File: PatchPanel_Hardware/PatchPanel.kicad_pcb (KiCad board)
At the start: 2 copper layers, 172.1 x 75.6 mm, 89 parts, among them Q1 Q_PMOS_DGS, Q10 Q_NMOS_DGS, Q11 Q_NMOS_DGS, Q12 Q_NMOS_DGS, Q13 Q_NMOS_DGS, Q14 Q_NMOS_DGS, Q15 Q_NMOS_DGS, Q16 Q_NMOS_DGS, Q17 Q_PMOS_DGS, Q18 Q_PMOS_DGS, Q19 Q_PMOS_DGS, Q2 Q_PMOS_DGS, Q20 Q_PMOS_DGS, Q21 Q_PMOS_DGS, Q22 Q_PMOS_DGS, Q23 Q_PMOS_DGS, Q24 Q_PMOS_DGS, Q25 Q_NMOS_DGS, Q26 Q_NMOS_DGS, Q27 Q_NMOS_DGS, Q28 Q_NMOS_DGS, Q29 Q_NMOS_DGS, Q3 Q_PMOS_DGS, Q30 Q_NMOS_DGS, Q31 Q_NMOS_DGS, Q32 Q_NMOS_DGS, Q4 Q_PMOS_DGS, Q5 Q_PMOS_DGS, Q6 Q_PMOS_DGS, Q7 Q_PMOS_DGS, Q8 Q_PMOS_DGS, Q9 Q_NMOS_DGS

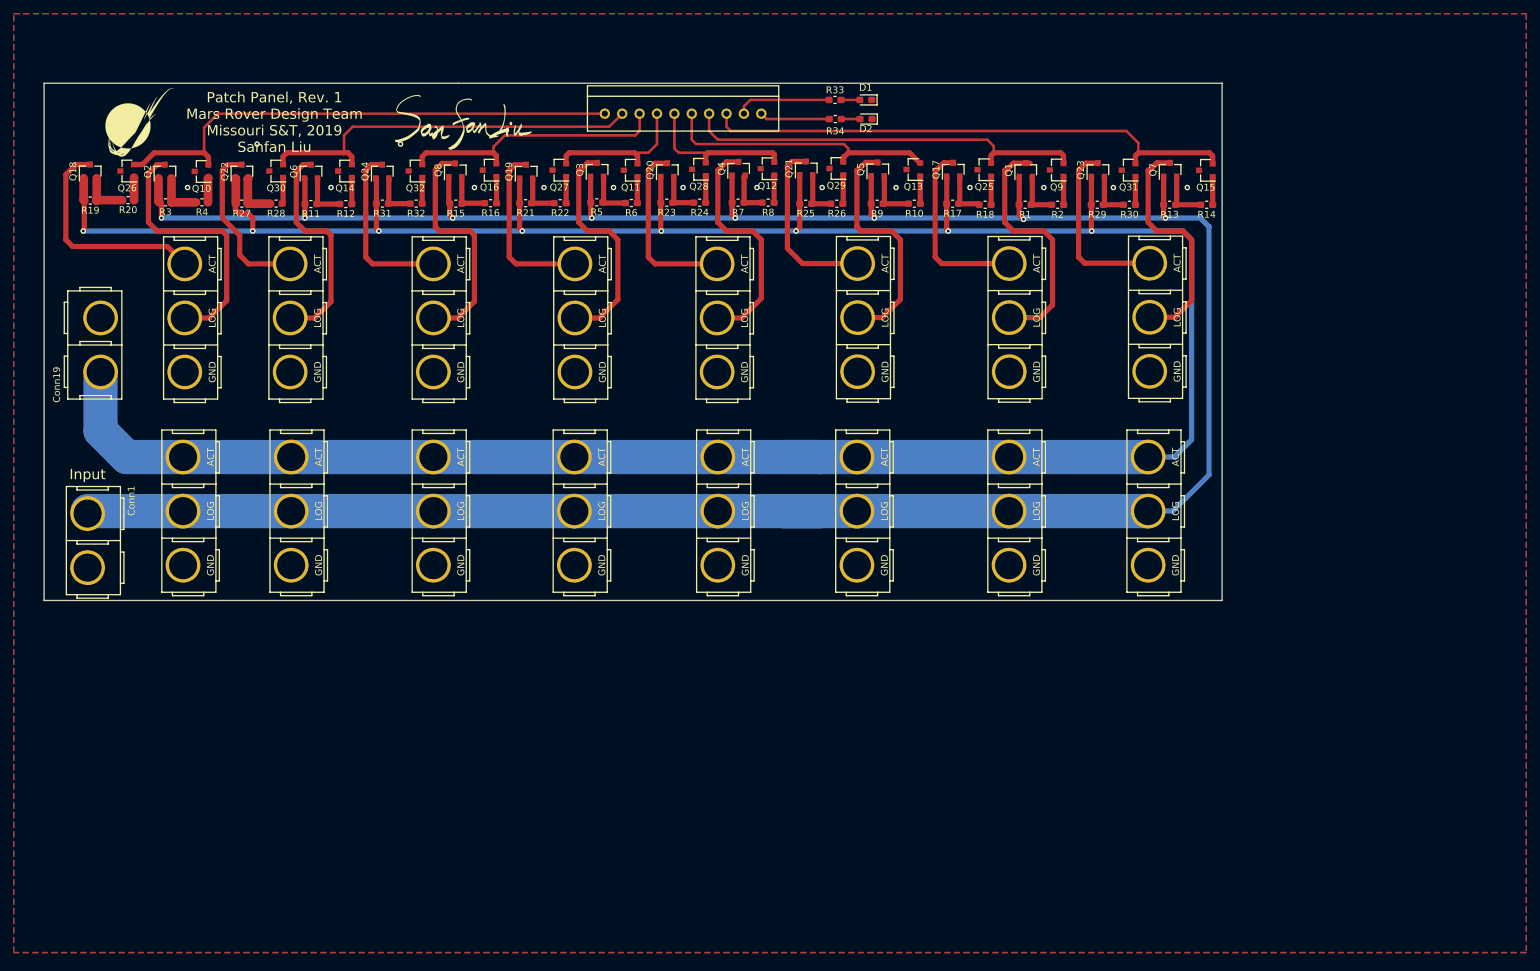
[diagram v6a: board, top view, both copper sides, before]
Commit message: fixed board review issue
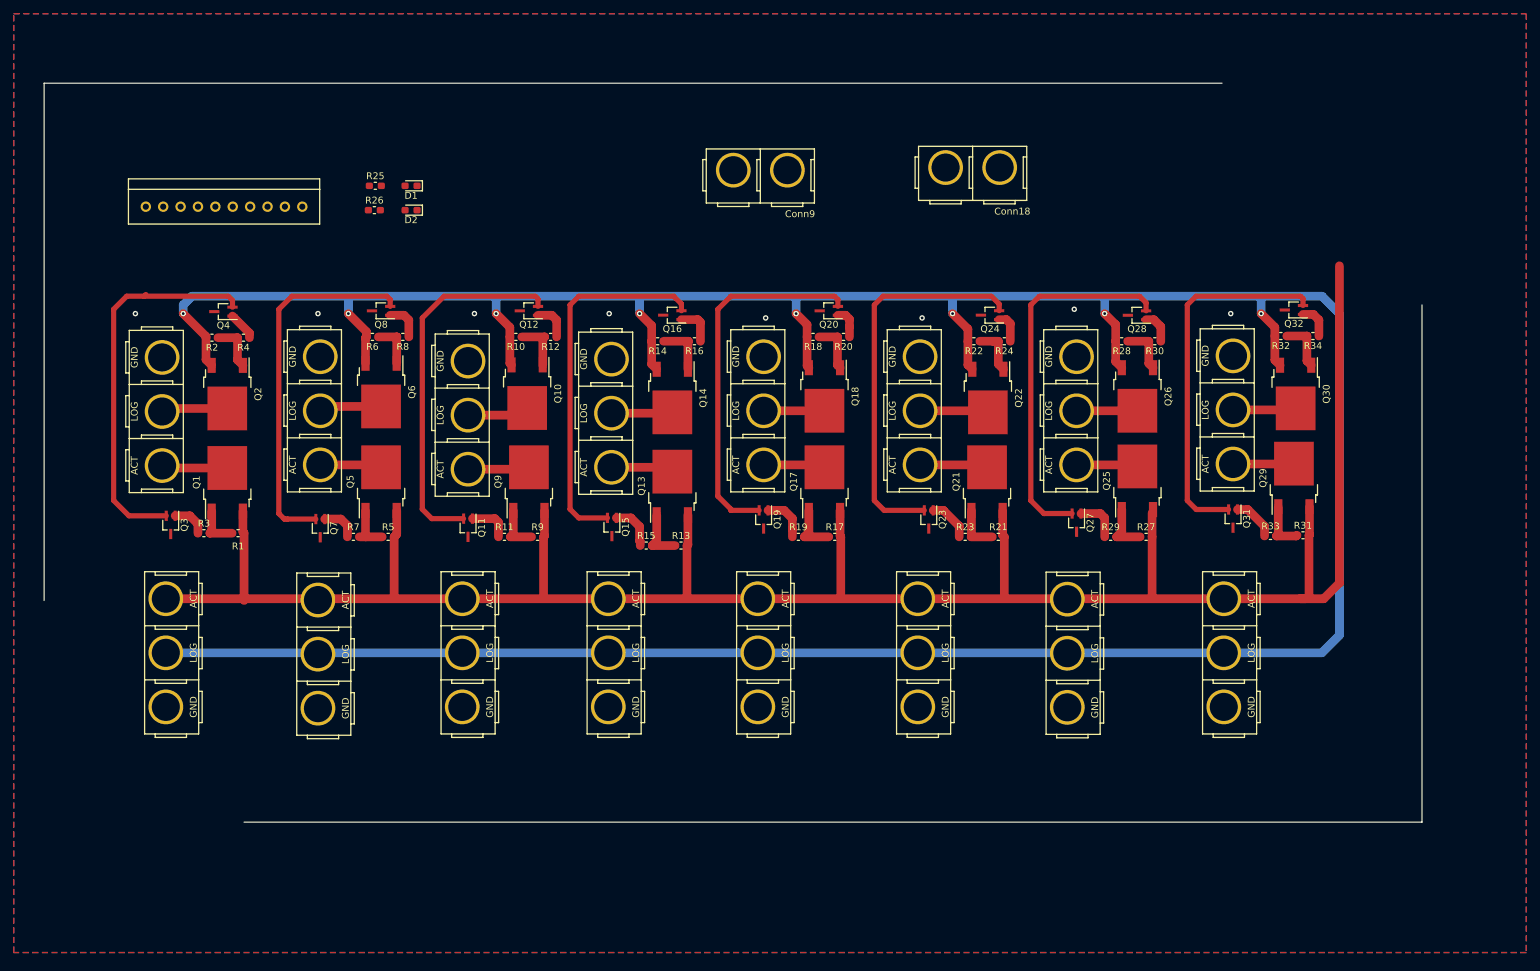
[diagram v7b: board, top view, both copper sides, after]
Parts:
- removed G***: LOGO, MRDT_Silkscreens:z_sig_SanfanLiu_sig21.8mmx12.3mm1
- removed G***: LOGO, MRDT_Silkscreens:0_MRDT_Logo_10mm
- Conn1: footprint MRDT_Connectors:Anderson_2_Vertical_Sidy_by_Side -> MRDT_Connectors:Anderson_3_Vertical_Side_by_Side
- Conn10: value Molex_SL_10 -> AndersonPP; footprint MRDT_Connectors:MOLEX_SL_10_Vertical -> MRDT_Connectors:Anderson_3_Vertical_Side_by_Side
- Conn18, Conn9: footprint MRDT_Connectors:Anderson_3_Vertical_Side_by_Side -> MRDT_Connectors:Anderson_2_Vertical_Sidy_by_Side
- Conn19: value AndersonPP -> Molex_SL_10; footprint MRDT_Connectors:Anderson_2_Vertical_Sidy_by_Side -> MRDT_Connectors:MOLEX_SL_10_Vertical
- Q1, Q17, Q18, Q2, Q21, Q22, Q5, Q6: footprint Package_TO_SOT_SMD:SOT-23 -> Package_TO_SOT_SMD:TO-252-2
- Q10, Q13, Q14, Q25, Q26, Q29, Q30, Q9: value Q_NMOS_DGS -> Q_PMOS_DGS; footprint Package_TO_SOT_SMD:SOT-23 -> Package_TO_SOT_SMD:TO-252-2
- Q11, Q12, Q15, Q16, Q27, Q28, Q31, Q32: footprint Package_TO_SOT_SMD:SOT-23 -> Package_TO_SOT_SMD:SOT-323_SC-70_Handsoldering
- Q19, Q20, Q23, Q24, Q3, Q4, Q7, Q8: value Q_PMOS_DGS -> Q_NMOS_DGS; footprint Package_TO_SOT_SMD:SOT-23 -> Package_TO_SOT_SMD:SOT-323_SC-70_Handsoldering
- R1, R10, R11, R12, R13, R14, R15, R16, R17, R18, R19, R2, R20, R21, R22, R23, R24, R27, R28, R29, R3, R30, R31, R32, R33, R34, R4, R5, R6, R7, R8, R9: value R -> 22k
- moved Q30 152.4 mm to (217.8, 80.3), turned to 270 degrees
- moved Q26 151.2 mm to (194.6, 80.7), turned to 270 degrees
- moved Conn15 145.0 mm to (57.5, 130.0)
- moved R31 143.0 mm to (218.8, 101.0), turned to 0 degrees
- moved R27 140.8 mm to (195.9, 101.2), turned to 0 degrees
- moved Q7 134.7 mm to (75.3, 99.9), turned to 270 degrees
- moved Q32 129.9 mm to (217.5, 68.0)
- moved R32 127.8 mm to (215.6, 71.9)
- moved Q1 125.3 mm to (61.7, 93.2)
- moved R28 125.2 mm to (192.3, 72.6)
- moved R2 125.1 mm to (59.4, 72.1)
- moved R1 124.6 mm to (63.3, 100.7), turned to 0 degrees
- moved R19 114.5 mm to (145.1, 101.2), turned to 0 degrees
- moved Q22 113.9 mm to (172.8, 80.9), turned to 270 degrees
- moved Q18 112.2 mm to (148.9, 80.7), turned to 270 degrees
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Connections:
- Conn1 pad 2: /Vlog -> Net-(Conn1-Pad2)
- Conn10 pad 1: Net-(Conn10-Pad1) -> GND
- Conn10 pad 2: Net-(Conn10-Pad2) -> /Vlog
- Conn10 pad 3: Net-(Conn10-Pad3) -> /Vact
- Conn18 pad 2: /Vlog -> /Vact
- Conn19 pad 1: GND -> /PL3
- Conn19 pad 2: /Vact -> /PL2
- Conn9 pad 2: Net-(Conn9-Pad2) -> /Vlog
- Q1 pad 1: /Vlog -> Net-(Q1-Pad1)
- Q1 pad 2: Net-(Q1-Pad2) -> Net-(Conn1-Pad3)
- Q1 pad 3: Net-(Conn2-Pad2) -> /Vact
- Q10 pad 2: Net-(Conn10-Pad1) -> Net-(Conn3-Pad2)
- Q10 pad 3: GND -> /Vlog
- Q11 pad 2: Net-(Conn10-Pad4) -> /PL1
- Q12 pad 2: Net-(Conn10-Pad5) -> /PL1
- Q13 pad 2: Net-(Conn10-Pad6) -> Net-(Conn4-Pad3)
- Q13 pad 3: GND -> /Vact
- Q14 pad 2: Net-(Conn10-Pad2) -> Net-(Conn4-Pad2)
- Q14 pad 3: GND -> /Vlog
- Q15 pad 2: Net-(Conn10-Pad8) -> /PL0
- Q16 pad 2: Net-(Conn10-Pad3) -> /PL0
- Q16 pad 3: GND -> Net-(Q16-Pad3)
- Q17 pad 1: /Vact -> Net-(Q17-Pad1)
- Q17 pad 2: Net-(Q17-Pad2) -> Net-(Conn5-Pad3)
- Q17 pad 3: Net-(Conn2-Pad3) -> /Vact
- Q18 pad 1: /Vact -> Net-(Q18-Pad1)
- Q18 pad 2: Net-(Q18-Pad2) -> Net-(Conn5-Pad2)
- Q18 pad 3: Net-(Conn3-Pad3) -> /Vlog
- Q19 pad 1: /Vact -> Net-(Q19-Pad1)
- Q19 pad 2: Net-(Q19-Pad2) -> /PL5
- Q19 pad 3: Net-(Conn4-Pad3) -> GND
- Q2 pad 1: /Vlog -> Net-(Q2-Pad1)
- Q2 pad 2: Net-(Q2-Pad2) -> Net-(Conn1-Pad2)
- Q2 pad 3: Net-(Conn3-Pad2) -> /Vlog
- Q20 pad 1: /Vact -> Net-(Q20-Pad1)
- Q20 pad 2: Net-(Q20-Pad2) -> /PL5
- Q20 pad 3: Net-(Conn5-Pad3) -> GND
- Q21 pad 1: /Vact -> Net-(Q21-Pad1)
- Q21 pad 2: Net-(Q21-Pad2) -> Net-(Conn6-Pad3)
- Q21 pad 3: Net-(Conn6-Pad3) -> /Vact
- Q22 pad 1: /Vact -> Net-(Q22-Pad1)
- Q22 pad 2: Net-(Q22-Pad2) -> Net-(Conn6-Pad2)
- Q22 pad 3: Net-(Conn7-Pad3) -> /Vlog
- Q23 pad 1: /Vact -> Net-(Q23-Pad1)
- Q23 pad 2: Net-(Q23-Pad2) -> /PL4
- Q23 pad 3: Net-(Conn8-Pad3) -> GND
- Q24 pad 1: /Vact -> Net-(Q24-Pad1)
- Q24 pad 2: Net-(Q24-Pad2) -> /PL4
- Q24 pad 3: Net-(Conn9-Pad3) -> GND
- Q25 pad 2: Net-(Conn10-Pad7) -> Net-(Conn7-Pad3)
- Q25 pad 3: GND -> /Vact
- Q26 pad 2: Net-(Conn10-Pad1) -> Net-(Conn7-Pad2)
- Q26 pad 3: GND -> /Vlog
- Q27 pad 2: Net-(Conn10-Pad4) -> /PG0
- Q28 pad 2: Net-(Conn10-Pad5) -> /PG0
- Q29 pad 2: Net-(Conn10-Pad6) -> Net-(Conn8-Pad3)
- Q29 pad 3: GND -> /Vact
- Q3 pad 1: /Vlog -> Net-(Q3-Pad1)
- Q3 pad 2: Net-(Q3-Pad2) -> /PL3
- Q3 pad 3: Net-(Conn4-Pad2) -> GND
- Q30 pad 2: Net-(Conn10-Pad2) -> Net-(Conn8-Pad2)
- Q30 pad 3: GND -> /Vlog
- Q31 pad 2: Net-(Conn10-Pad8) -> /PF3
- Q32 pad 2: Net-(Conn10-Pad3) -> /PF3
- Q4 pad 1: /Vlog -> Net-(Q4-Pad1)
- Q4 pad 2: Net-(Q4-Pad2) -> /PL3
- Q4 pad 3: Net-(Conn5-Pad2) -> GND
- Q5 pad 1: /Vlog -> Net-(Q5-Pad1)
- Q5 pad 2: Net-(Q5-Pad2) -> Net-(Conn2-Pad3)
- Q5 pad 3: Net-(Conn6-Pad2) -> /Vact
- Q6 pad 1: /Vlog -> Net-(Q6-Pad1)
- Q6 pad 2: Net-(Q6-Pad2) -> Net-(Conn2-Pad2)
- Q6 pad 3: Net-(Conn7-Pad2) -> /Vlog
- Q7 pad 1: /Vlog -> Net-(Q7-Pad1)
- Q7 pad 2: Net-(Q7-Pad2) -> /PL2
- Q7 pad 3: Net-(Conn8-Pad2) -> GND
- Q8 pad 1: /Vlog -> Net-(Q8-Pad1)
- Q8 pad 2: Net-(Q8-Pad2) -> /PL2
- Q8 pad 3: Net-(Conn9-Pad2) -> GND
- Q9 pad 2: Net-(Conn10-Pad7) -> Net-(Conn3-Pad3)
- Q9 pad 3: GND -> /Vact
- R1 pad 1: Net-(Q1-Pad2) -> Net-(Q1-Pad1)
- R1 pad 2: /Vlog -> /Vact
- R10 pad 1: Net-(Q13-Pad1) -> Net-(Q10-Pad1)
- R10 pad 2: Net-(Q5-Pad2) -> /Vlog
- R11 pad 1: Net-(Q6-Pad2) -> Net-(Q11-Pad1)
- R11 pad 2: /Vlog -> Net-(Q9-Pad1)
- R12 pad 1: Net-(Q14-Pad1) -> Net-(Q12-Pad1)
- R12 pad 2: Net-(Q6-Pad2) -> Net-(Q10-Pad1)
- R13 pad 1: Net-(Q7-Pad2) -> Net-(Q13-Pad1)
- R13 pad 2: /Vlog -> /Vact
- R14 pad 1: Net-(Q15-Pad1) -> Net-(Q14-Pad1)
- R14 pad 2: Net-(Q7-Pad2) -> /Vlog
- R15 pad 1: Net-(Q8-Pad2) -> Net-(Q15-Pad1)
- R15 pad 2: /Vlog -> Net-(Q13-Pad1)
- R16 pad 2: Net-(Q8-Pad2) -> Net-(Q14-Pad1)
- R17 pad 1: Net-(Q17-Pad2) -> Net-(Q17-Pad1)
- R18 pad 1: Net-(Q25-Pad1) -> Net-(Q18-Pad1)
- R18 pad 2: Net-(Q17-Pad2) -> /Vlog
- R19 pad 1: Net-(Q18-Pad2) -> Net-(Q19-Pad1)
- R19 pad 2: /Vact -> Net-(Q17-Pad1)
- R2 pad 1: Net-(Q9-Pad1) -> Net-(Q2-Pad1)
- R2 pad 2: Net-(Q1-Pad2) -> /Vlog
- R20 pad 1: Net-(Q26-Pad1) -> Net-(Q20-Pad1)
- R20 pad 2: Net-(Q18-Pad2) -> Net-(Q18-Pad1)
- R21 pad 1: Net-(Q19-Pad2) -> Net-(Q21-Pad1)
- R22 pad 1: Net-(Q27-Pad1) -> Net-(Q22-Pad1)
- R22 pad 2: Net-(Q19-Pad2) -> /Vlog
- R23 pad 1: Net-(Q20-Pad2) -> Net-(Q23-Pad1)
- R23 pad 2: /Vact -> Net-(Q21-Pad1)
- R24 pad 1: Net-(Q28-Pad1) -> Net-(Q24-Pad1)
- R24 pad 2: Net-(Q20-Pad2) -> Net-(Q22-Pad1)
- R25 pad 1: Net-(Q21-Pad2) -> /PF2
- R25 pad 2: /Vact -> Net-(D1-Pad2)
- R26 pad 1: Net-(Q29-Pad1) -> /PF1
- R26 pad 2: Net-(Q21-Pad2) -> Net-(D2-Pad2)
- R27 pad 1: Net-(Q22-Pad2) -> Net-(Q25-Pad1)
- R28 pad 1: Net-(Q30-Pad1) -> Net-(Q26-Pad1)
- R28 pad 2: Net-(Q22-Pad2) -> /Vlog
- R29 pad 1: Net-(Q23-Pad2) -> Net-(Q27-Pad1)
- R29 pad 2: /Vact -> Net-(Q25-Pad1)
- R3 pad 1: Net-(Q2-Pad2) -> Net-(Q3-Pad1)
- R3 pad 2: /Vlog -> Net-(Q1-Pad1)
- R30 pad 1: Net-(Q31-Pad1) -> Net-(Q28-Pad1)
- R30 pad 2: Net-(Q23-Pad2) -> Net-(Q26-Pad1)
- R31 pad 1: Net-(Q24-Pad2) -> Net-(Q29-Pad1)
- R32 pad 1: Net-(Q32-Pad1) -> Net-(Q30-Pad1)
- R32 pad 2: Net-(Q24-Pad2) -> /Vlog
- R33 pad 1: Net-(Conn10-Pad9) -> Net-(Q31-Pad1)
- R33 pad 2: Net-(D1-Pad2) -> Net-(Q29-Pad1)
- R34 pad 1: Net-(Conn10-Pad10) -> Net-(Q32-Pad1)
- R34 pad 2: Net-(D2-Pad2) -> Net-(Q30-Pad1)
- R4 pad 1: Net-(Q10-Pad1) -> Net-(Q4-Pad1)
- R4 pad 2: Net-(Q2-Pad2) -> Net-(Q2-Pad1)
- R5 pad 1: Net-(Q3-Pad2) -> Net-(Q5-Pad1)
- R5 pad 2: /Vlog -> /Vact
- R6 pad 1: Net-(Q11-Pad1) -> Net-(Q6-Pad1)
- R6 pad 2: Net-(Q3-Pad2) -> /Vlog
- R7 pad 1: Net-(Q4-Pad2) -> Net-(Q7-Pad1)
- R7 pad 2: /Vlog -> Net-(Q5-Pad1)
- R8 pad 1: Net-(Q12-Pad1) -> Net-(Q8-Pad1)
- R8 pad 2: Net-(Q4-Pad2) -> Net-(Q6-Pad1)
- R9 pad 1: Net-(Q5-Pad2) -> Net-(Q9-Pad1)
- R9 pad 2: /Vlog -> /Vact
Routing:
- net /Vact: track 433.3 -> 321.6 mm, vias 8 -> 0
- net Net-(Conn10-Pad8): track 78.4 -> 0.00 mm
- net Net-(Conn10-Pad1): track 76.1 -> 0.00 mm
- net /Vlog: track 410.6 -> 479.9 mm
- net Net-(Conn10-Pad7): track 59.2 -> 0.00 mm
- net Net-(Conn10-Pad2): track 57.3 -> 0.00 mm
- net /PL4: track 0.00 -> 56.7 mm
- net /PL3: track 0.00 -> 56.3 mm
- net /PG0: track 0.00 -> 54.3 mm
- net /PL0: track 0.00 -> 54.1 mm
- net /PL1: track 0.00 -> 54.0 mm
- net /PL2: track 0.00 -> 53.8 mm
- net /PL5: track 0.00 -> 53.8 mm
- net /PF3: track 0.00 -> 53.7 mm
- net Net-(Conn10-Pad6): track 40.7 -> 0.00 mm
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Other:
- board size 172.1 x 75.6 mm -> 201.3 x 108 mm
- board text removed: "Input"
- board text removed: "Patch Panel, Rev. 1 Mars Rover Design Team Missouri S&T, 2019 Sanfan Liu"

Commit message: matching
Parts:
- moved Conn19 133.1 mm to (194.3, 54.6)
- moved D1 130.8 mm to (219.3, 51.2)
- moved D2 130.8 mm to (219.3, 54.7)
- moved R25 130.8 mm to (214.1, 51.2)
- moved R26 130.8 mm to (214.0, 54.7)
- moved Conn9 81.7 mm to (50.7, 63.2)
- moved Conn18 31.4 mm to (133.2, 63.0)
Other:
- board size 201.3 x 108 mm -> 194.3 x 97.2 mm
